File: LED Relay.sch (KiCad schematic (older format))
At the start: 43 parts, among them J1 TEST_1P, J2 TEST_1P, J3 TEST_1P, J4 TEST_1P, J5 TEST_1P, J6 TEST_1P, J7 TEST_1P, J8 TEST_1P, J9 Header, U1 LT3014IDD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

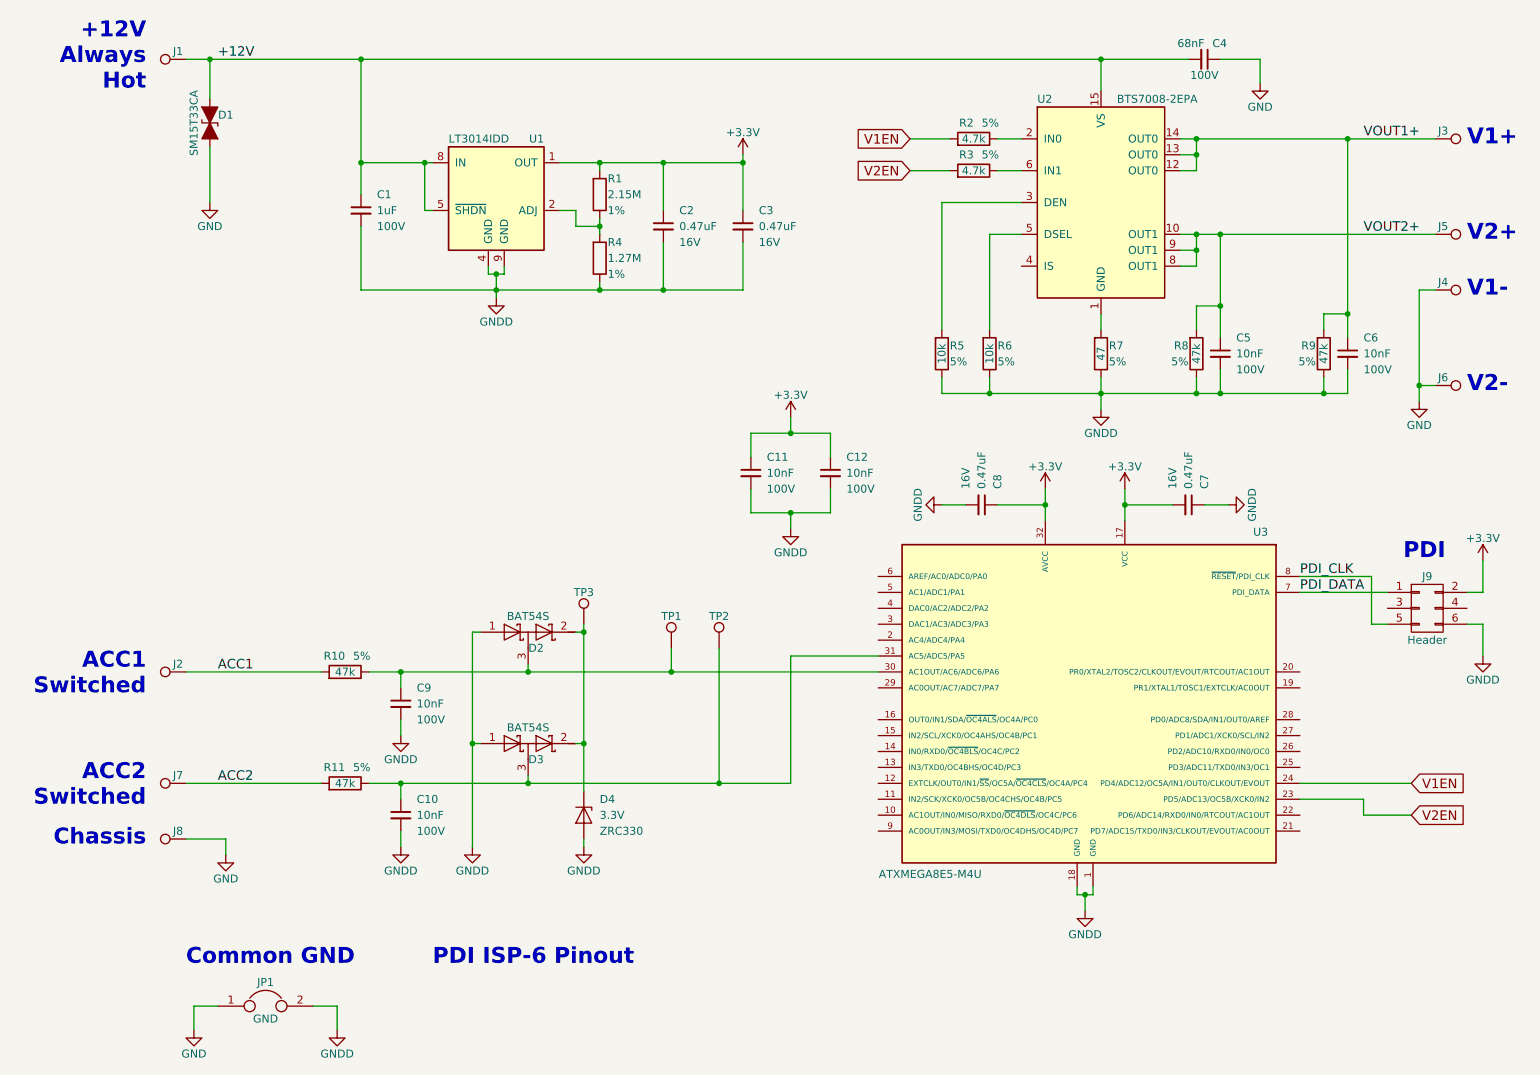
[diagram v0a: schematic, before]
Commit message: Upped Rev to 2.1. Added R12 and R13. Moved connections on micro-controller.
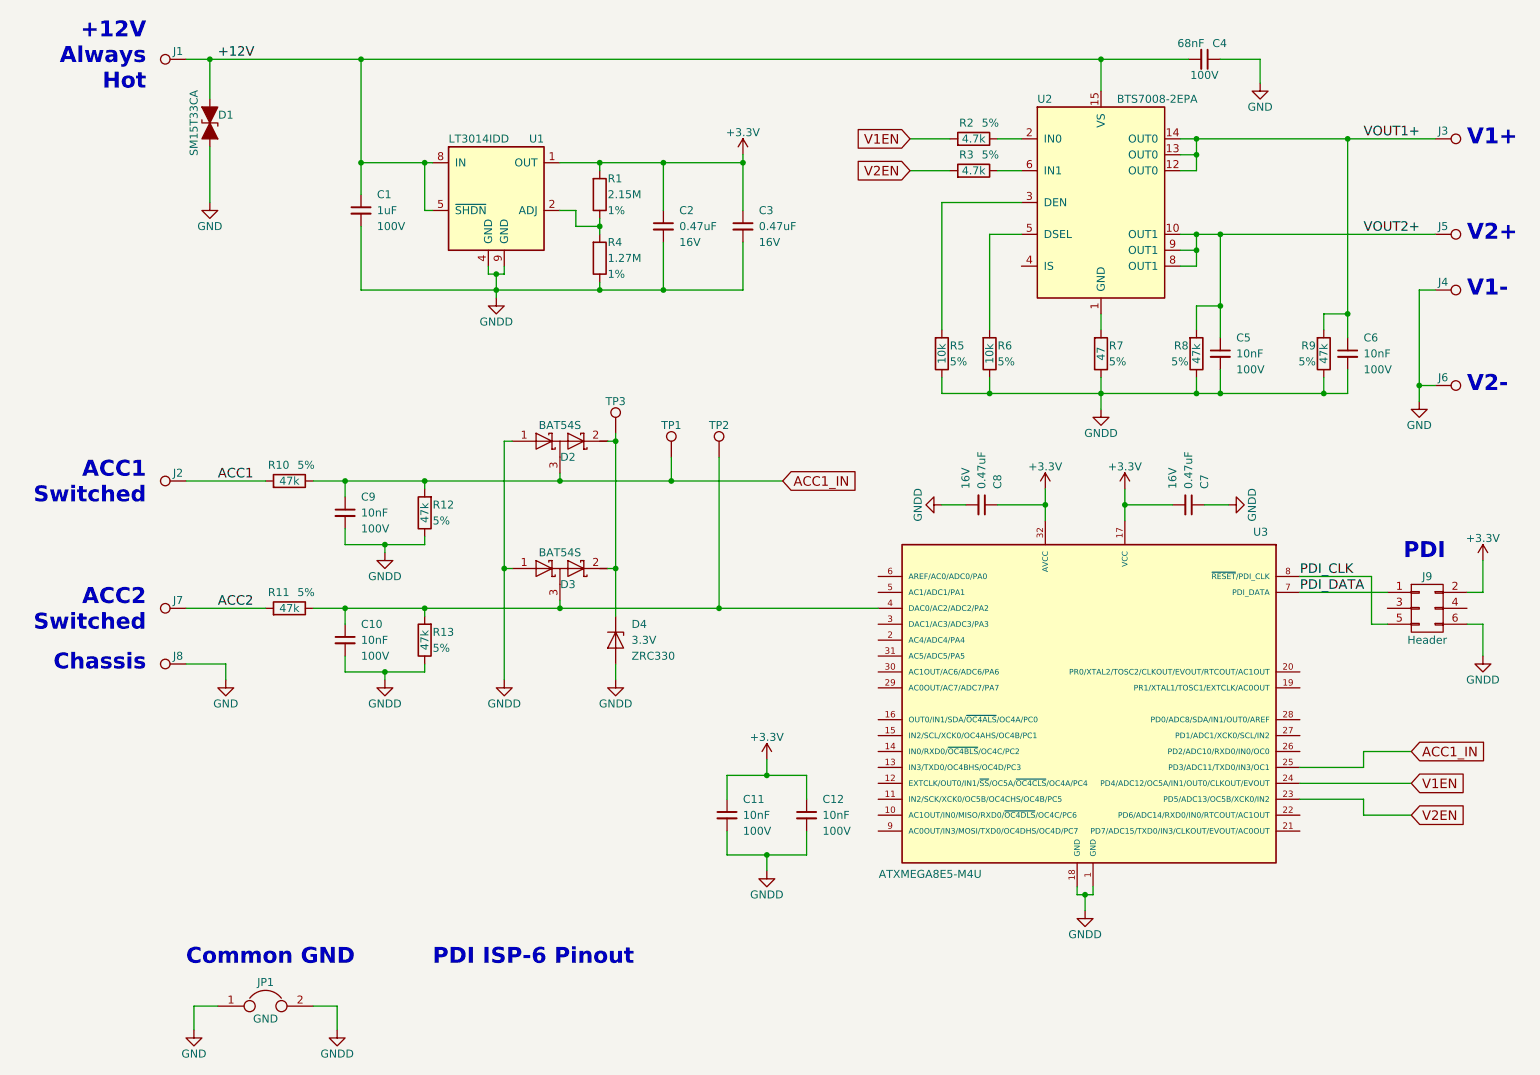
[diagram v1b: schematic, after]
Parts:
- added R12, R13: 47k, Resistors_SMD:R_0603, symbol R
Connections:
- net GNDD: now also R12.1, R13.1
- net ACC1_IN: now reaches U3.25 (PD3/ADC11/TXD0/IN3/OC1)
- net ACC1_IN: now also C9.1, D2.3 (common), R10.1, TP1.1, R12.2
- net at C10.1, D3.3 (common), R11.1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: now also U3.4 (DAC0/AC2/ADC2/PA2), R13.2; no longer U3.31 (AC5/ADC5/PA5)
- now unconnected: U3.30 (AC1OUT/AC6/ADC6/PA6)
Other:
- moved on the sheet: C10, C11, C12, C9, D2, D3, D4, J2, J7, J8, R10, R11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
